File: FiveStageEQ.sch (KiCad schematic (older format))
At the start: 75 parts, among them J1 AudioJack3, J2 AudioJack3, U1 OPAMP, U2 OPAMP, U3 OPAMP, U4 OPAMP, U5 OPAMP, U6 OPAMP, U7 OPAMP, U8 LM317_TO3

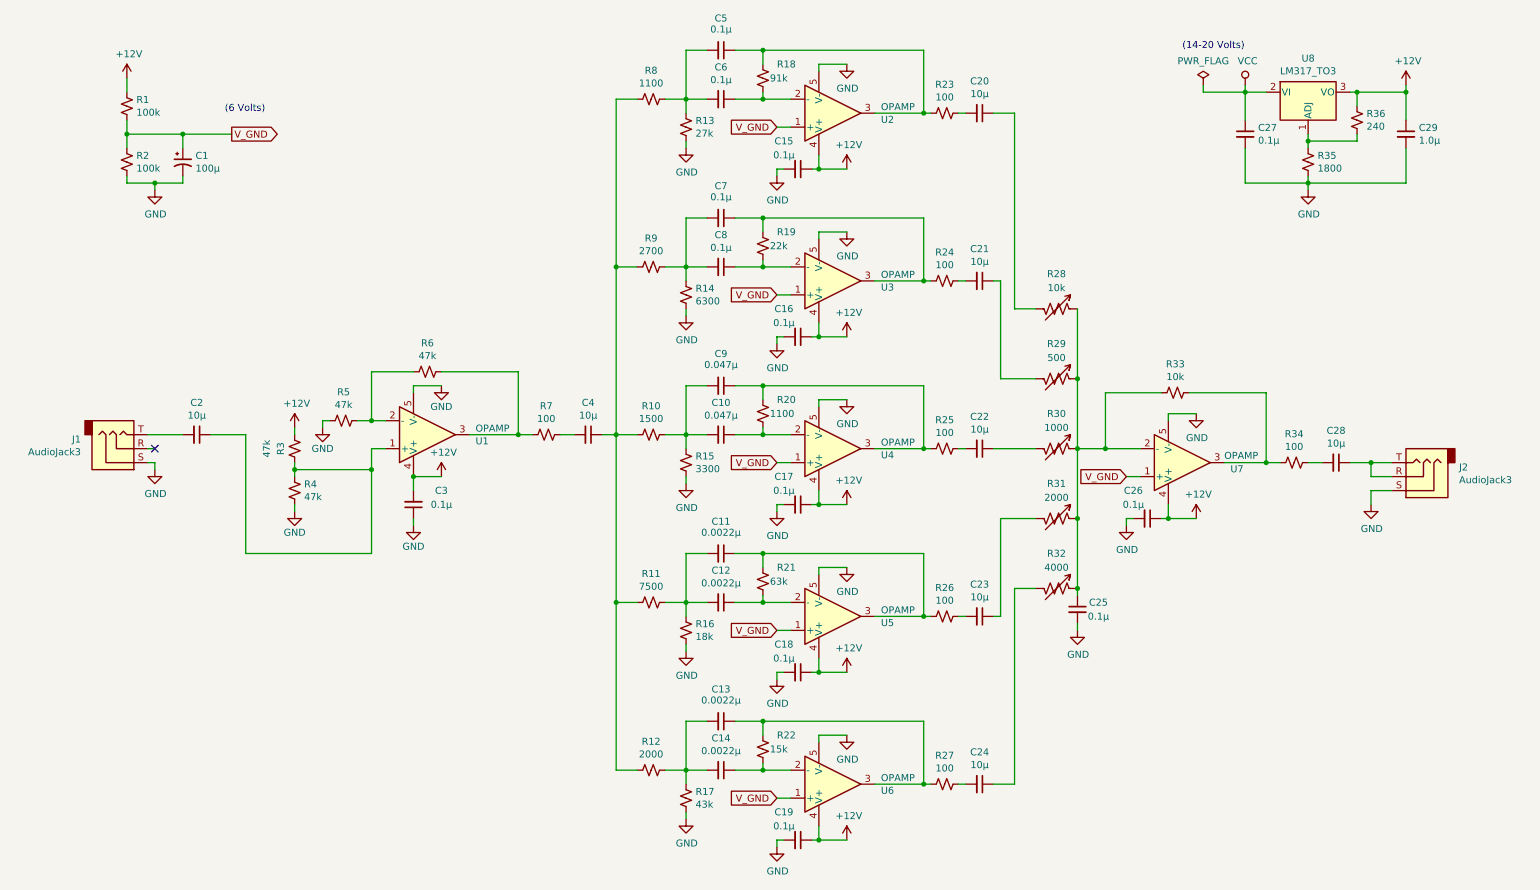
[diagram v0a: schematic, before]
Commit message: Created LM833 Symbol
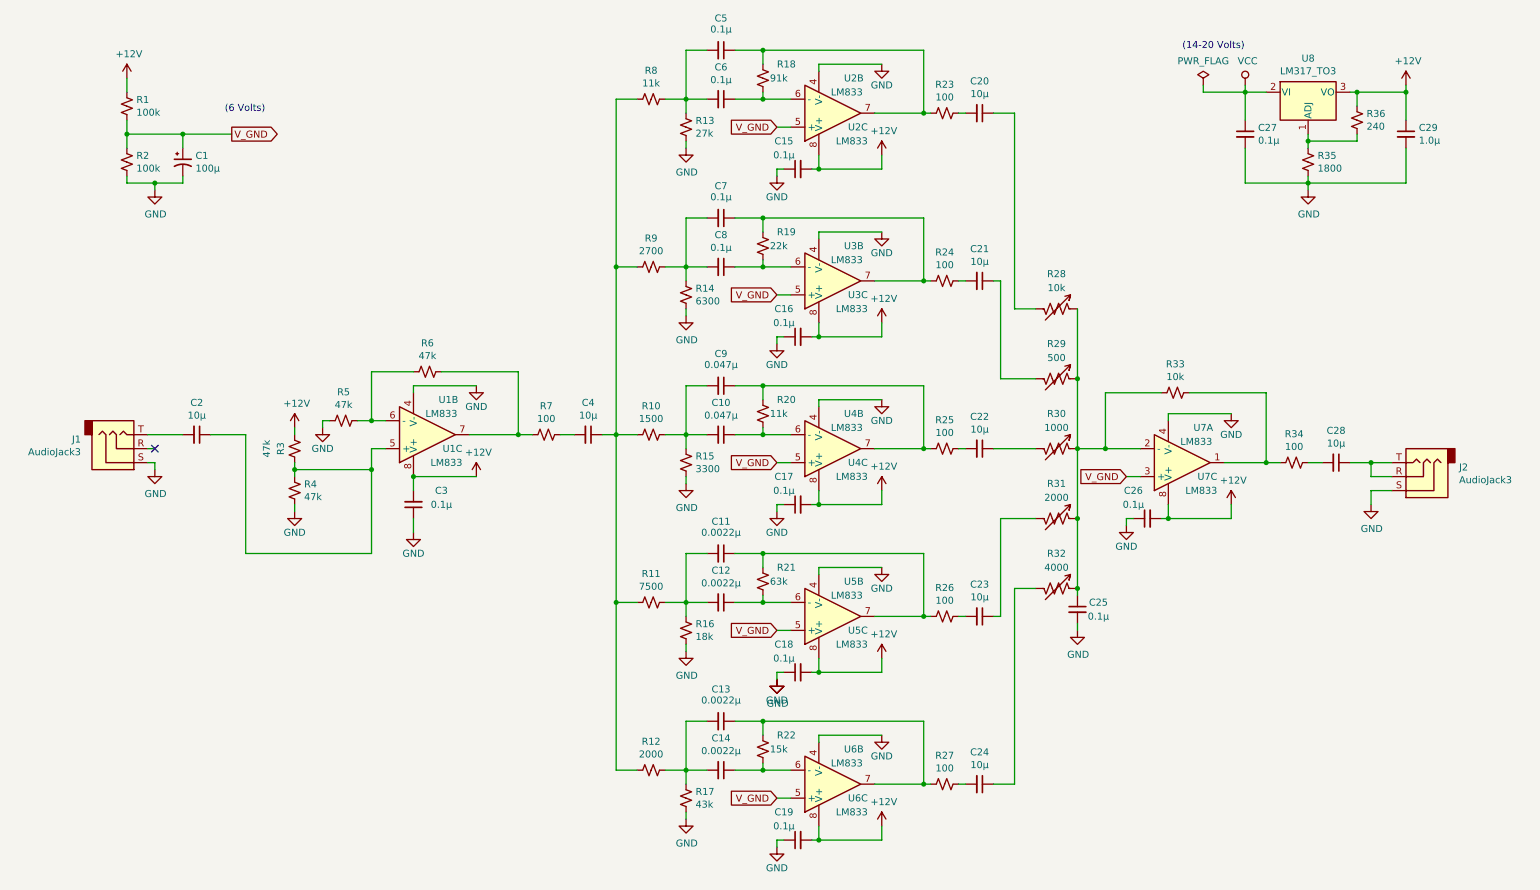
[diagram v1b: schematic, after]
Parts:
- removed U1, U2, U3, U4, U5, U6, U7: OPAMP, Package_TO_SOT_SMD:SOT-23-5, symbol pspice:OPAMP
- added U1, U2, U3, U4, U5, U6, U7: LM833, symbol Custom:LM833
- R20, R8: value 1100 -> 11k
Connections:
- net +12V: now also C15.2, C16.2, C17.2, C18.2, C19.2, C26.2, U1.8 (V+), U2.8 (V+), U3.8 (V+), U4.8 (V+), U5.8 (V+), U6.8 (V+), U7.8 (V+); no longer C15.1, C16.1, C17.1, C18.1, C19.1, C26.1
- net GND: now also C15.1, C16.1, C17.1, C18.1, C19.1, C26.1, U1.4 (V-), U2.4 (V-), U3.4 (V-), U4.4 (V-), U5.4 (V-), U6.4 (V-), U7.4 (V-); no longer C15.2, C16.2, C17.2, C18.2, C19.2, C26.2
- net V_GND: now also U2.5 (+), U3.5 (+), U4.5 (+), U5.5 (+), U6.5 (+), U7.3 (+)
- net at C6.1, R18.1: now also U2.6 (-)
- net at C5.1, R18.2, R23.1: now also U2.7
- net at C25.1, R28.1, R29.1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: now also U7.2 (-)
- net at C2.1, R3.2, R4.2: now also U1.5 (+)
- net at R5.2, R6.1: now also U1.6 (-)
- net at R6.2, R7.1: now also U1.7
- net at C8.1, R19.1: now also U3.6 (-)
- net at C7.1, R19.2, R24.1: now also U3.7
- net at C10.1, R20.1: now also U4.6 (-)
- net at C9.1, R20.2, R25.1: now also U4.7
- net at C12.1, R21.1: now also U5.6 (-)
- net at C11.1, R21.2, R26.1: now also U5.7
- net at C14.1, R22.1: now also U6.6 (-)
- net at C13.1, R22.2, R27.1: now also U6.7
- net at R33.2, R34.1: now also U7.1
